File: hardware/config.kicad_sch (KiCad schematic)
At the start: 40 parts, among them IC1 74LVC1G04GM,115, IC2 74LVC2G00HK3-7, J4 JTAG, SW1 219-2MST, U4 GateMate-CCGM1A1, U9 AT25QL321-MBUE-T

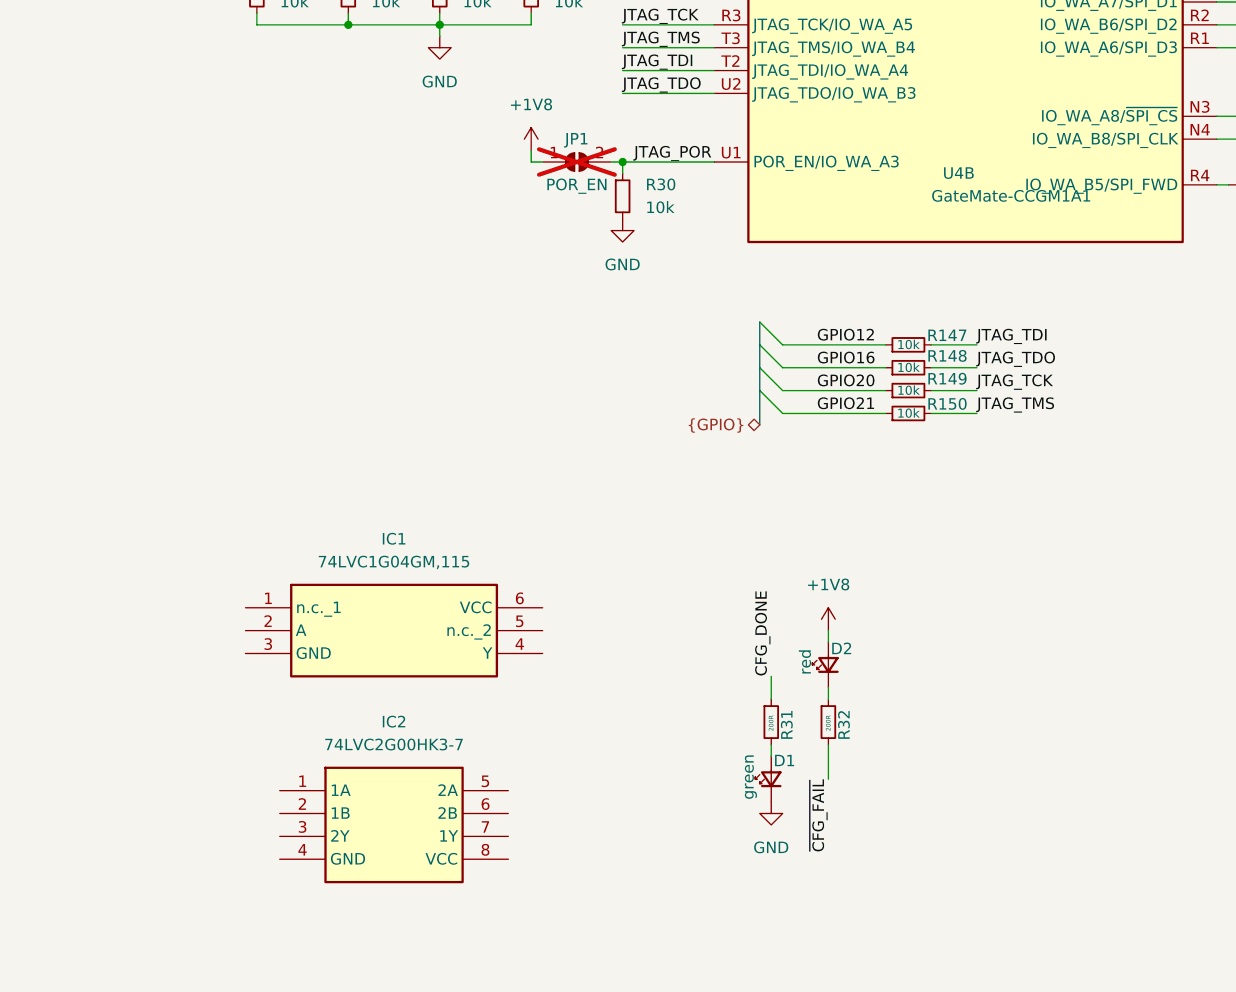
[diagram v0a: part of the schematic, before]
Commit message: fix #26 fix #24
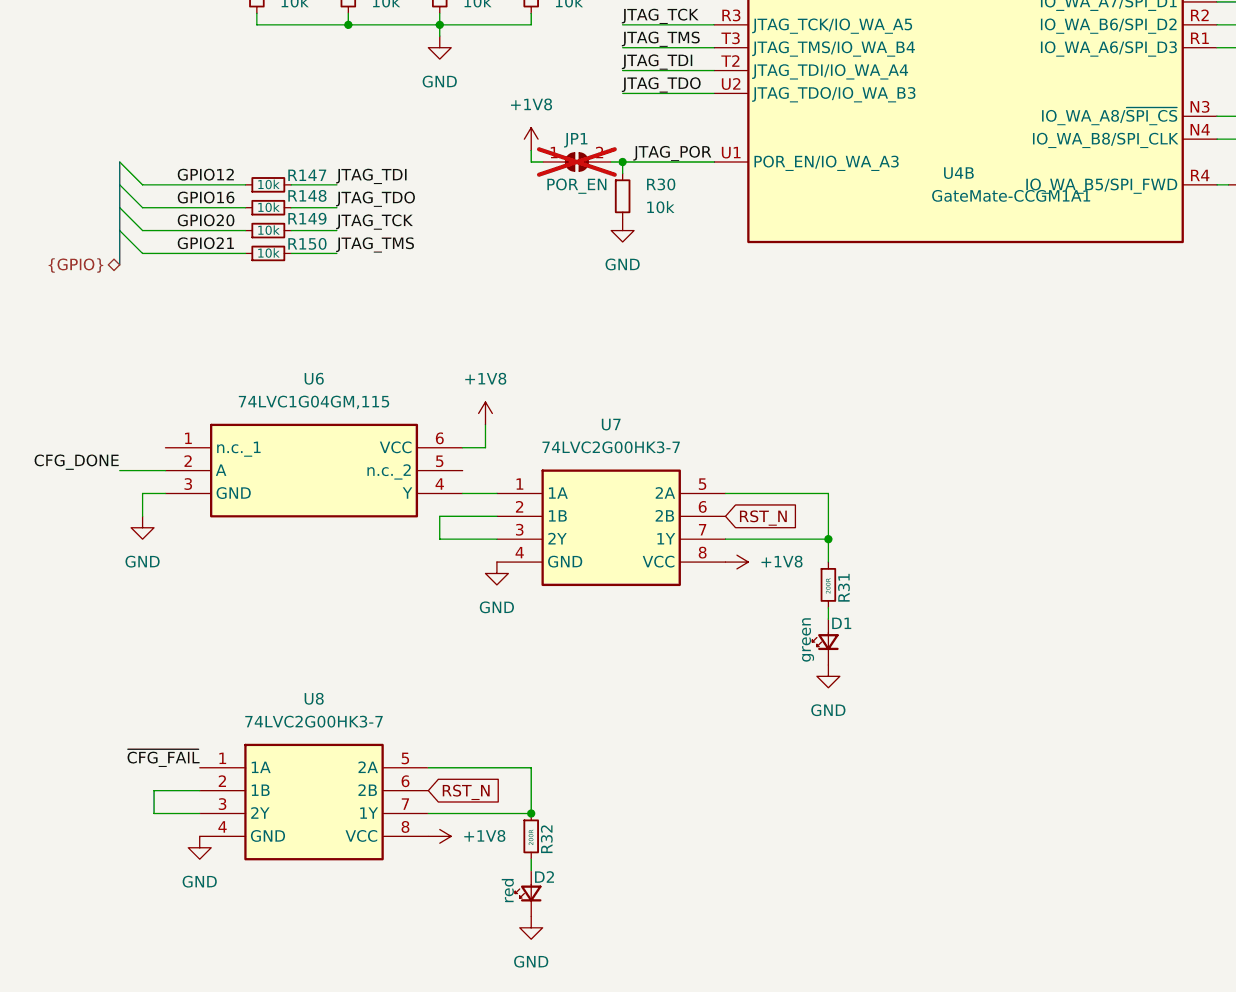
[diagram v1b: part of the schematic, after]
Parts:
- added U8: 74LVC2G00HK3-7, 74LVC2G00HK3-7:74LVC2G00HK37, symbol 74LVC2G00HK3-7:74LVC2G00HK3-7
- renumbered IC1 to U6, IC2 to U7
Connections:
- net +1V8: now also U6.6 (VCC), U7.8 (VCC), U8.8 (VCC); no longer D2.2 (A)
- net CFG_DONE: now also U6.2 (A); no longer R31.1
- net GND: now also D2.1 (K), U6.3 (GND), U7.4 (GND), U8.4 (GND)
- net ~{CFG_FAIL}: now also U8.1 (1A); no longer R32.2
- net at R32.1: now also U8.5 (2A), U8.7 (1Y); no longer D2.1 (K)
- net at U6.4 (Y): now also U7.1 (1A)
- net at U7.2 (1B): now also U7.3 (2Y)
- net at U7.5 (2A): now also R31.1, U7.7 (1Y)
- net RST_N: now reaches U7.6 (2B)
- net RST_N: now also U8.6 (2B)
- new net: D2.2 (A), R32.2
- new net: U8.2 (1B), U8.3 (2Y)
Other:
- moved on the sheet: D1, D2, R147, R148, R149, R150, R31, R32, U6, U7

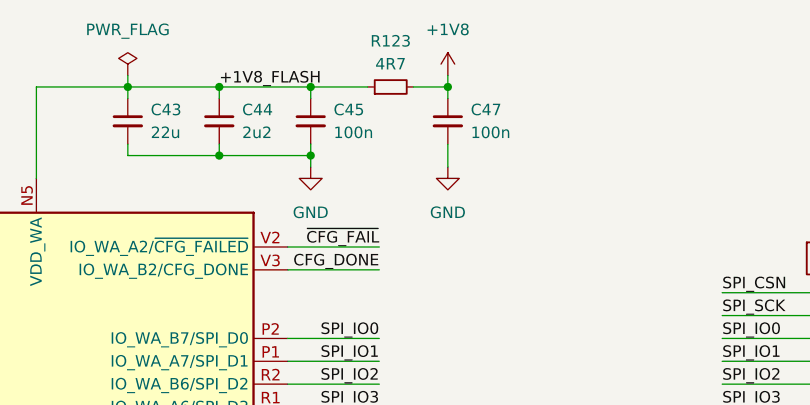
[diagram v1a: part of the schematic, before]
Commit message: power: removed rc filters from gpio domains
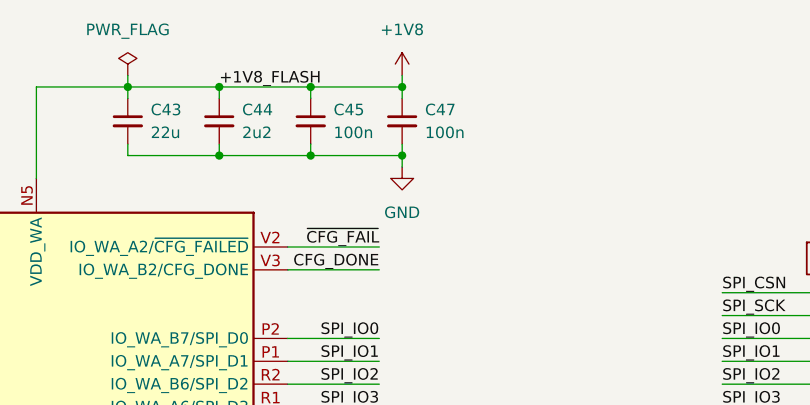
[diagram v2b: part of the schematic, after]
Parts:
- removed R123: 4R7, Resistor_SMD:R_0402_1005Metric, symbol Device:R_Small
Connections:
- net +1V8_FLASH is gone; now on net +1V8: C43.1, C44.1, C45.1, U4.N5 (VDD_WA), U4.P3 (VDD_WA), U4.P5 (VDD_WA), U4.T1 (VDD_WA), U4.U3 (VDD_WA)
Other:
- moved on the sheet: C47
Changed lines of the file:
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@@
 	)
 	(junction
-		(at 66.04 62.23)
+		(at 149.86 59.69)
 		(diameter 0)
 		(color 0 0 0 0)
 	)
 	(junction
-		(at 149.86 59.69)
+		(at 66.04 62.23)
 		(diameter 0)
 		(color 0 0 0 0)
@@
 	)
 	(junction
-		(at 165.1 52.07)
+		(at 160.02 52.07)
 		(diameter 0)
 		(color 0 0 0 0)
@@
 	)
 	(junction
+		(at 160.02 59.69)
+		(diameter 0)
+		(color 0 0 0 0)
+	)
+	(junction
 		(at 71.12 69.85)
 		(diameter 0)
@@
 	(wire
 		(pts
-			(xy 149.86 59.69) (xy 149.86 60.96)
-		)
-		(stroke
-			(width 0)
-			(type default)
-		)
-	)
-	(wire
-		(pts
 			(xy 66.04 62.23) (xy 71.12 62.23)
 		)
@@
 	(wire
 		(pts
+			(xy 149.86 59.69) (xy 160.02 59.69)
+		)
+		(stroke
+			(width 0)
+			(type default)
+		)
+	)
+	(wire
+		(pts
 			(xy 17.78 73.66) (xy 17.78 74.93)
 		)
@@
 	(wire
 		(pts
+			(xy 160.02 59.69) (xy 160.02 60.96)
+		)
+		(stroke
+			(width 0)
+			(type default)
+		)
+	)
+	(wire
+		(pts
 			(xy 195.58 129.54) (xy 205.74 129.54)
 		)
@@
 	(wire
 		(pts
-			(xy 165.1 52.07) (xy 165.1 53.34)
+			(xy 160.02 52.07) (xy 160.02 53.34)
 		)
 		(stroke
@@
 	(wire
 		(pts
-			(xy 149.86 52.07) (xy 156.21 52.07)
+			(xy 149.86 52.07) (xy 160.02 52.07)
 		)
 		(stroke
@@
 	(wire
 		(pts
-			(xy 165.1 58.42) (xy 165.1 60.96)
+			(xy 160.02 58.42) (xy 160.02 59.69)
 		)
 		(stroke
@@
 	(wire
 		(pts
-			(xy 165.1 50.8) (xy 165.1 52.07)
+			(xy 160.02 50.8) (xy 160.02 52.07)
 		)
 		(stroke
@@
 	(wire
 		(pts
-			(xy 161.29 52.07) (xy 165.1 52.07)
-		)
-		(stroke
-			(width 0)
-			(type default)
-		)
-	)
-	(wire
-		(pts
 			(xy 205.74 87.63) (xy 205.74 73.66)
 		)
@@
 		(lib_name "+1V8_4")
 		(lib_id "power:+1V8")
-		(at 165.1 50.8 0)
+		(at 160.02 50.8 0)
 		(unit 1)
 		(exclude_from_sim no)
@@
 		(fields_autoplaced yes)
 		(property "Reference" "#PWR062"
-			(at 165.1 54.61 0)
+			(at 160.02 54.61 0)
 			(effects
 				(font
@@
 		)
 		(property "Value" "+1V8"
-			(at 165.1 45.72 0)
+			(at 160.02 45.72 0)
 			(effects
 				(font
@@
 		)
 		(property "Footprint" ""
-			(at 165.1 50.8 0)
+			(at 160.02 50.8 0)
 			(effects
 				(font
@@
 		)
 		(property "Datasheet" ""
-			(at 165.1 50.8 0)
+			(at 160.02 50.8 0)
 			(effects
 				(font
@@
 		)
 		(property "Description" "Power symbol creates a global label with name \"+1V8\""
-			(at 165.1 50.8 0)
+			(at 160.02 50.8 0)
 			(effects
 				(font
@@
 	)
 	(symbol
-		(lib_id "power:GND")
-		(at 149.86 60.96 0)
-		(unit 1)
-		(exclude_from_sim no)
-		(in_bom yes)
-		(on_board yes)
-		(dnp no)
-		(fields_autoplaced yes)
-		(property "Reference" "#PWR0139"
-			(at 149.86 67.31 0)
-			(effects
-				(font
-					(size 1.27 1.27)
-				)
-				(hide yes)
-			)
-		)
-		(property "Value" "GND"
-			(at 149.86 66.04 0)
-			(effects
-				(font
-					(size 1.27 1.27)
-				)
-			)
-		)
-		(property "Footprint" ""
-			(at 149.86 60.96 0)
-			(effects
-				(font
-					(size 1.27 1.27)
-				)
-				(hide yes)
-			)
-		)
-		(property "Datasheet" ""
-			(at 149.86 60.96 0)
-			(effects
-				(font
-					(size 1.27 1.27)
-				)
-				(hide yes)
-			)
-		)
-		(property "Description" "Power symbol creates a global label with name \"GND\" , ground"
-			(at 149.86 60.96 0)
-			(effects
-				(font
-					(size 1.27 1.27)
-				)
-				(hide yes)
-			)
-		)
-		(pin "1"
-		)
-		(instances
-			(project "gatemate-plm"
-				(path "/9e5cbfd6-8186-4817-919e-acd256336bc8/1fc2f15e-8369-4c6d-a2f1-3c85144bfcff"
-					(reference "#PWR0139")
-					(unit 1)
-				)
-			)
-		)
-	)
-	(symbol
 		(lib_id "Device:R_Small")
 		(at 226.06 133.35 0)
@@
 	(symbol
 		(lib_id "Device:C_Small")
-		(at 165.1 55.88 0)
+		(at 160.02 55.88 0)
 		(unit 1)
 		(exclude_from_sim no)
@@
 		(fields_autoplaced yes)
 		(property "Reference" "C47"
-			(at 167.64 54.6163 0)
+			(at 162.56 54.6163 0)
 			(effects
 				(font
@@
 		)
 		(property "Value" "100n"
-			(at 167.64 57.1563 0)
+			(at 162.56 57.1563 0)
 			(effects
 				(font
@@
 		)
 		(property "Footprint" "Capacitor_SMD:C_0402_1005Metric"
-			(at 165.1 55.88 0)
+			(at 160.02 55.88 0)
 			(effects
 				(font
@@
 		)
 		(property "Datasheet" "~"
-			(at 165.1 55.88 0)
+			(at 160.02 55.88 0)
 			(effects
 				(font
@@
 		)
 		(property "Description" ""
-			(at 165.1 55.88 0)
+			(at 160.02 55.88 0)
 			(effects
 				(font
@@
 	(symbol
 		(lib_id "power:GND")
-		(at 165.1 60.96 0)
+		(at 160.02 60.96 0)
 		(unit 1)
 		(exclude_from_sim no)
@@
 		(fields_autoplaced yes)
 		(property "Reference" "#PWR063"
-			(at 165.1 67.31 0)
+			(at 160.02 67.31 0)
 			(effects
 				(font
@@
 		)
 		(property "Value" "GND"
-			(at 165.1 66.04 0)
+			(at 160.02 66.04 0)
 			(effects
 				(font
@@
 		)
 		(property "Footprint" ""
-			(at 165.1 60.96 0)
+			(at 160.02 60.96 0)
 			(effects
 				(font
@@
 		)
 		(property "Datasheet" ""
-			(at 165.1 60.96 0)
+			(at 160.02 60.96 0)
 			(effects
 				(font
@@
 		)
 		(property "Description" "Power symbol creates a global label with name \"GND\" , ground"
-			(at 165.1 60.96 0)
+			(at 160.02 60.96 0)
 			(effects
 				(font
@@
 					(unit 1)
 				)
-			)
-		)
-	)
-	(symbol
-		(lib_id "Device:R_Small")
-		(at 158.75 52.07 90)
-		(unit 1)
-		(exclude_from_sim no)
-		(in_bom yes)
-		(on_board yes)
-		(dnp no)
-		(property "Reference" "R123"
-			(at 158.75 46.99 90)
-			(effects
-				(font
-					(size 1.27 1.27)
-				)
-			)
-		)
-		(property "Value" "4R7"
-			(at 158.75 49.53 90)
-			(effects
-				(font
-					(size 1.27 1.27)
-				)
-			)
-		)
-		(property "Footprint" "Resistor_SMD:R_0402_1005Metric"
-			(at 158.75 52.07 0)
-			(effects
-				(font
-					(size 1.27 1.27)
-				)
-				(hide yes)
-			)
-		)
-		(property "Datasheet" "~"
-			(at 158.75 52.07 0)
-			(effects
-				(font
-					(size 1.27 1.27)
-				)
-				(hide yes)
-			)
-		)
-		(property "Description" "Resistor, small symbol"
-			(at 158.75 52.07 0)
-			(effects
-				(font
-					(size 1.27 1.27)
-				)
-				(hide yes)
-			)
-		)
-		(pin "1"
-		)
-		(pin "2"
-		)
-		(instances
-			(project "gatemate-plm"
-				(path "/9e5cbfd6-8186-4817-919e-acd256336bc8/1fc2f15e-8369-4c6d-a2f1-3c85144bfcff"
-					(reference "R123")
-					(unit 1)
-				)

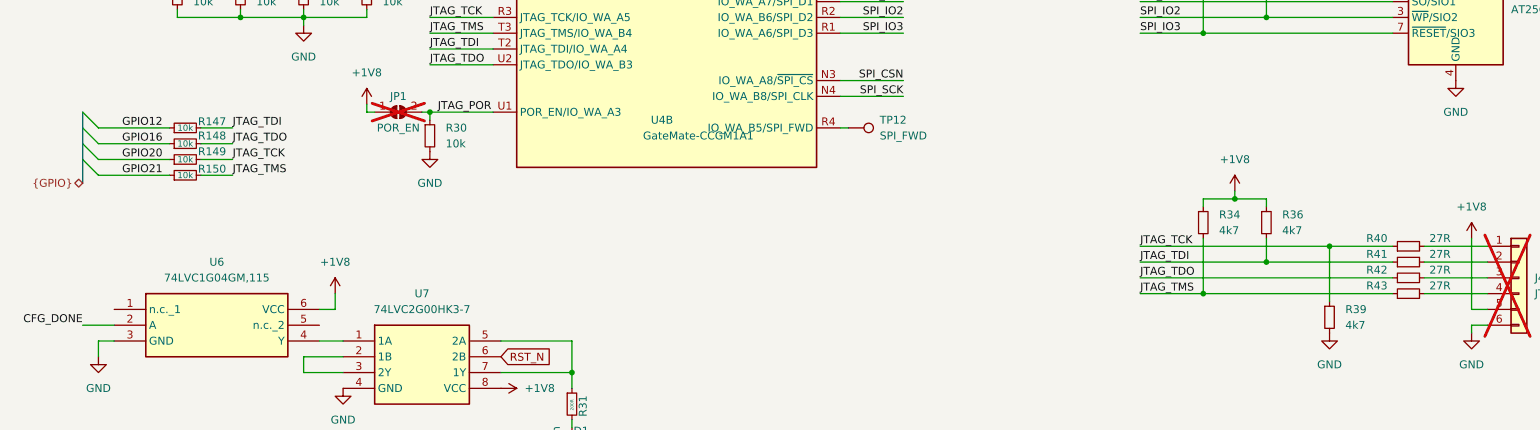
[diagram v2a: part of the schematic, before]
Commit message: config: remove jtag header
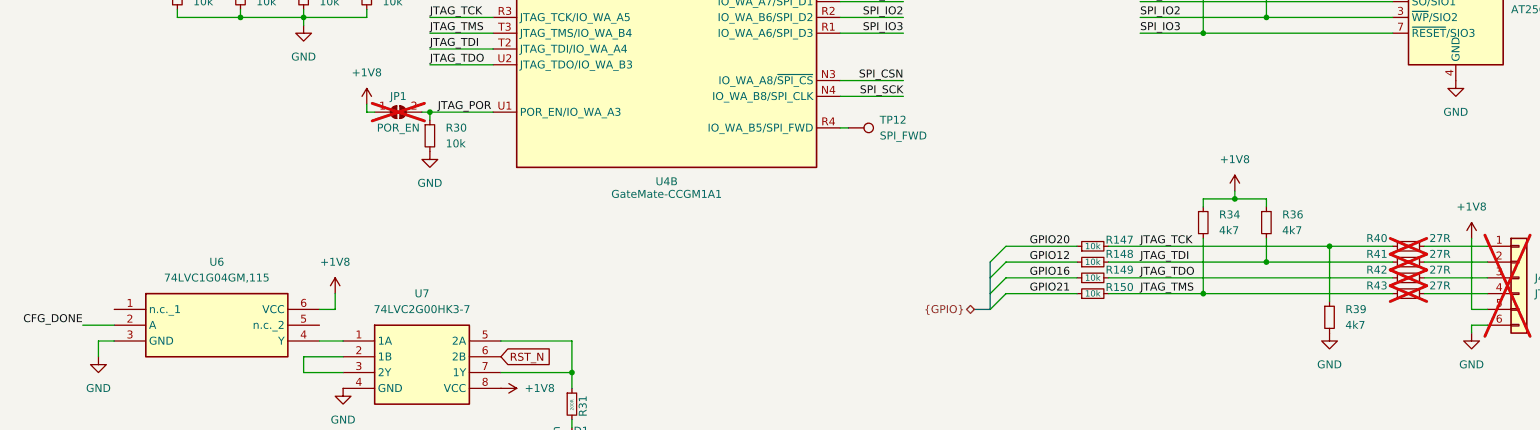
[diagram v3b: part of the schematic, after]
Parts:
- R40, R41, R42, R43: now not fitted
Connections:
- net GPIO12: now also R148.1; no longer R147.1
- net GPIO16: now also R149.1; no longer R148.1
- net GPIO20: now also R147.1; no longer R149.1
- net JTAG_TCK: now also R147.2; no longer R149.2
- net JTAG_TDI: now also R148.2; no longer R147.2
- net JTAG_TDO: now also R149.2; no longer R148.2
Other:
- moved on the sheet: R147, R148, R149, R150
